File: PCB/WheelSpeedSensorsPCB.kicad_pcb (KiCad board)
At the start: 2 copper layers, 60 x 90 mm, 21 parts, among them J1 RearLeftWheel, J10 FrontRightShock, J11 RearRightShock, J2 FrontRightWheel, J3 RearRightWheel, J4 Conn_01x02_Pin, J5 FrontLeftWheel, J6 RearLeftShock, J7 VehicleBus, J8 Conn_01x02_Pin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

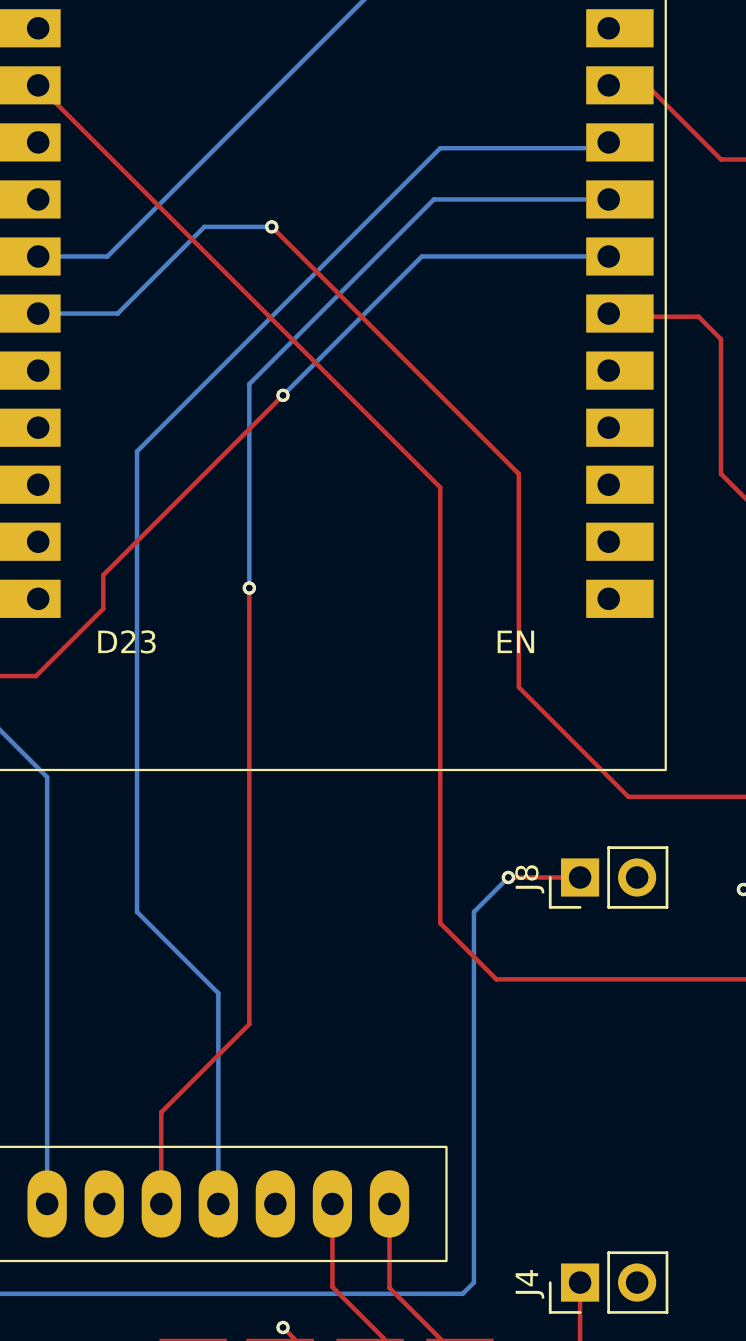
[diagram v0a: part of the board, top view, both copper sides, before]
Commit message: Fix schematic/PCB to use proper CAN TX and RX pins
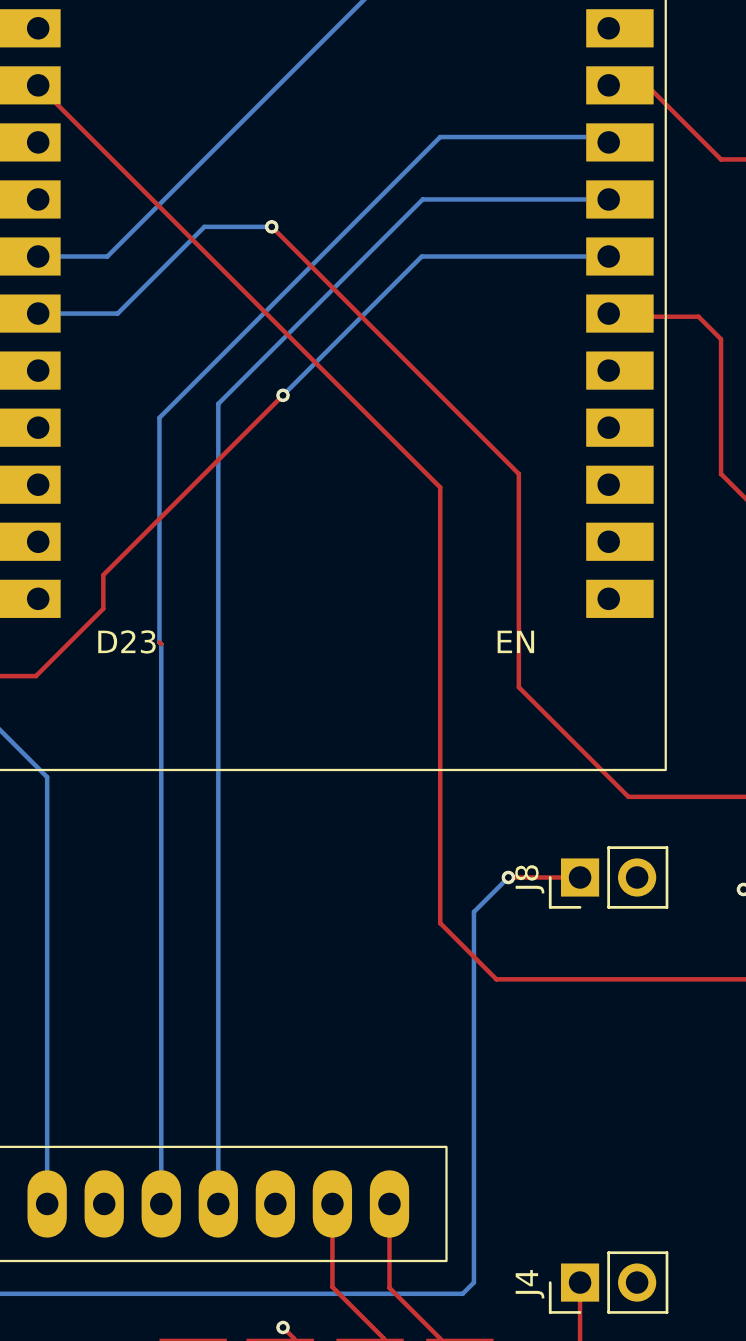
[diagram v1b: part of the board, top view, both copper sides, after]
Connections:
- U4 pad 3: Net-(U3-D25) -> Net-(U3-D26)
- U4 pad 4: Net-(U3-D26) -> Net-(U3-D25)
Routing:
- net Net-(U3-D26): track 61.7 -> 60.8 mm
- net Net-(U3-D25): track 57.5 -> 56.8 mm, vias 1 -> 0
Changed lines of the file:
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@@
 			(layers "*.Cu" "*.Mask")
 			(remove_unused_layers no)
-			(net 24 "Net-(U3-D25)")
+			(net 28 "Net-(U3-D26)")
 			(pinfunction "RX")
 			(pintype "input")
@@
 			(layers "*.Cu" "*.Mask")
 			(remove_unused_layers no)
-			(net 28 "Net-(U3-D26)")
+			(net 24 "Net-(U3-D25)")
 			(pinfunction "TX")
 			(pintype "input")
@@
 	)
 	(segment
-		(start 127.58 123.42)
+		(start 139.22 82.78)
+		(end 147.5 82.78)
+		(width 0.2)
+		(layer "B.Cu")
+		(net 24)
+	)
+	(segment
+		(start 130.12 91.88)
+		(end 139.22 82.78)
+		(width 0.2)
+		(layer "B.Cu")
+		(net 24)
+	)
+	(segment
+		(start 130.12 127.5)
+		(end 130.12 91.88)
+		(width 0.2)
+		(layer "B.Cu")
+		(net 24)
+	)
+	(segment
+		(start 127.5 102.5)
+		(end 127.58 102.58)
+		(width 0.2)
+		(layer "F.Cu")
+		(net 28)
+	)
+	(segment
+		(start 127.5 102.5)
+		(end 127.58 102.58)
+		(width 0.2)
+		(layer "B.Cu")
+		(net 28)
+	)
+	(segment
+		(start 127.58 102.58)
 		(end 127.58 127.5)
 		(width 0.2)
-		(layer "F.Cu")
-		(net 24)
-	)
-	(segment
-		(start 131.5 100.08)
-		(end 131.5 119.5)
-		(width 0.2)
-		(layer "F.Cu")
-		(net 24)
-	)
-	(segment
-		(start 131.5 119.5)
-		(end 127.58 123.42)
-		(width 0.2)
-		(layer "F.Cu")
-		(net 24)
-	)
-	(via
-		(at 131.5 100.08)
-		(size 0.6)
-		(drill 0.3)
-		(layers "F.Cu" "B.Cu")
-		(net 24)
-	)
-	(segment
-		(start 131.5 100.08)
-		(end 131.5 91)
-		(width 0.2)
-		(layer "B.Cu")
-		(net 24)
-	)
-	(segment
-		(start 139.72 82.78)
-		(end 147.5 82.78)
-		(width 0.2)
-		(layer "B.Cu")
-		(net 24)
-	)
-	(segment
-		(start 131.5 91)
-		(end 139.72 82.78)
-		(width 0.2)
-		(layer "B.Cu")
-		(net 24)
-	)
-	(segment
-		(start 130.12 118.12)
-		(end 130.12 127.5)
-		(width 0.2)
 		(layer "B.Cu")
 		(net 28)
 	)
 	(segment
-		(start 126.5 114.5)
-		(end 130.12 118.12)
+		(start 147.26 80)
+		(end 147.5 80.24)
 		(width 0.2)
 		(layer "B.Cu")
@@
 	)
 	(segment
-		(start 140 80.5)
-		(end 147.24 80.5)
+		(start 127.5 102.5)
+		(end 127.5 92.5)
 		(width 0.2)
 		(layer "B.Cu")
@@
 	)
 	(segment
-		(start 126.5 114.5)
-		(end 126.5 102)
-		(width 0.2)
-		(layer "B.Cu")
-		(net 28)
-	)
-	(segment
-		(start 126.5 102)
-		(end 126.5 94)
-		(width 0.2)
-		(layer "B.Cu")
-		(net 28)
-	)
-	(segment
-		(start 126.5 94)
-		(end 140 80.5)
+		(start 140 80)
+		(end 147.26 80)
 		(width 0.2)
 		(layer "B.Cu")
@@
 		(width 0.2)
 		(layer "B.Cu")
+		(net 28)
+	)
+	(segment
+		(start 127.5 92.5)
+		(end 140 80)
+		(width 0.2)
+		(layer "B.Cu")
